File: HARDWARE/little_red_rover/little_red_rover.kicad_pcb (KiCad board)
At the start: 2 copper layers, 127.3 x 82.2 mm, 50 parts, among them J1 USB_C_Receptacle_USB2.0_14P, J2 Conn_01x04_Socket, J3 Conn_01x02_Socket, J4 Conn_01x02_Socket, J5 Conn_01x01_Socket, J6 Conn_01x01_Socket, U1 ESP32-C3-MINI-1, U2 BQ24230RGT, U3 MIC5504-3.3YM5, U4 TPS613222ADBV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

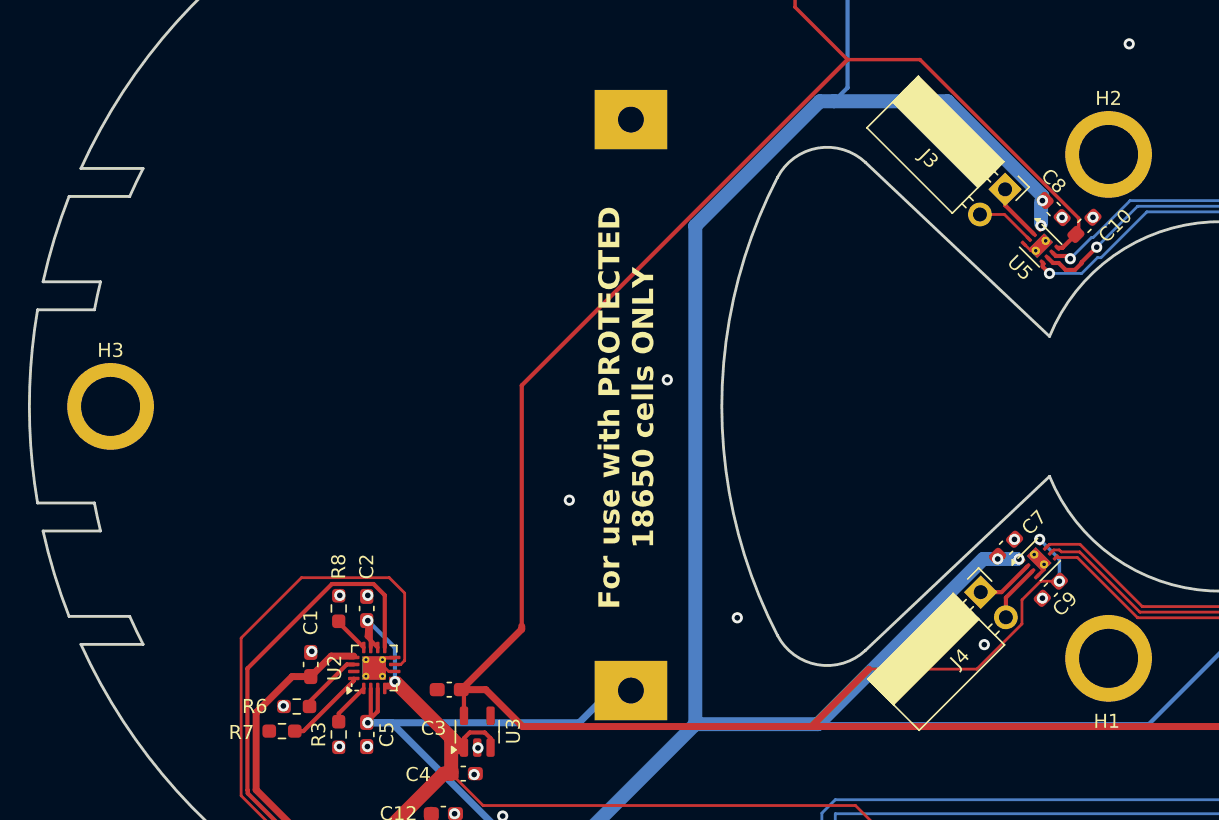
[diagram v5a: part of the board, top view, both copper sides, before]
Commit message: Fix threaded inserts not being included in BOM / placement
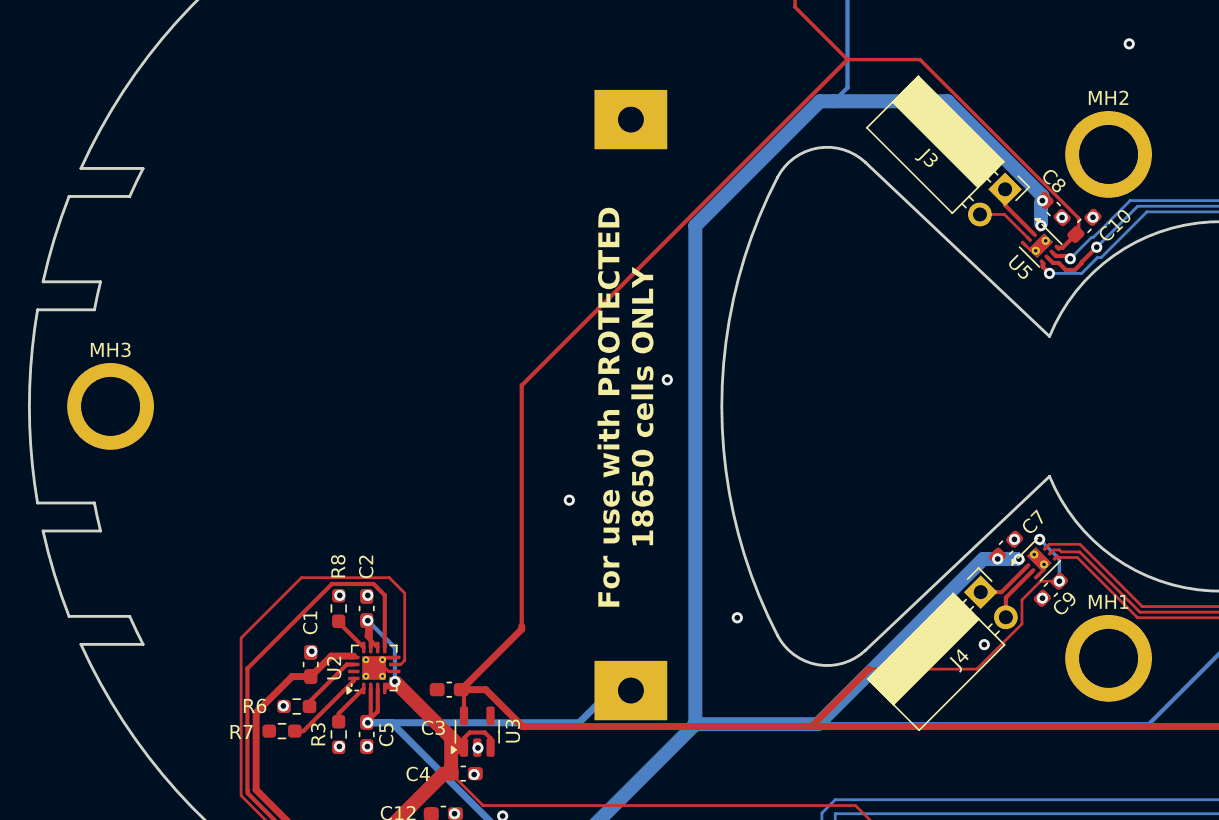
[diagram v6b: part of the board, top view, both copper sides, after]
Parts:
- removed H1, H2, H3: MountingHole, digikey_imports:m3_threaded_insert
- added MH1: M3_threaded, digikey_imports:m3_threaded_insert, F.Cu at (163.5, 117.9)
- added MH2: M3_threaded, digikey_imports:m3_threaded_insert, F.Cu at (163.5, 81.9)
- added MH3: M3_threaded, digikey_imports:m3_threaded_insert, F.Cu at (92.2, 99.9)
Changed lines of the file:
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@@
       (drillshape 0)
       (scaleselection 1)
-      (outputdirectory "gerbers/")
+      (outputdirectory "../pcb_fabrication_files/gerbers/")
     )
   )
@@
     (tags "capacitor handsolder")
     (property "JLC" "0603")
-    (property "LCSC" "C19666")
+    (property "LCSC" "")
     (property "Sheetfile" "little_red_rover.kicad_sch")
     (property "Sheetname" "")
@@
       (rotate (xyz 0 0 0))
     )
+  )
+  (footprint "digikey_imports:m3_threaded_insert" (layer "F.Cu")
+    (at 163.524805 117.9)
+    (property "JLC" "-")
+    (property "LCSC" "C5301780")
+    (property "Sheetfile" "little_red_rover.kicad_sch")
+    (property "Sheetname" "")
+    (property "ki_description" "Mounting Hole without connection")
+    (property "ki_keywords" "mounting hole")
+    (attr smd)
+    (fp_text reference "MH1" (at 0 -4 unlocked) (layer "F.SilkS")
+        (effects (font (size 1 1) (thickness 0.1)))
+    )
+    (fp_text value "M3_threaded" (at 0 4 unlocked) (layer "F.Fab")
+        (effects (font (size 1 1) (thickness 0.15)))
+    )
+    (fp_text user "${REFERENCE}" (at 0 6 unlocked) (layer "F.Fab")
+        (effects (font (size 1 1) (thickness 0.15)))
+    )
+    (pad "" np_thru_hole circle (at 0 0) (size 6.2 6.2) (drill 4.22) (layers "F&B.Cu" "*.Mask"))
   )
   (footprint "Capacitor_SMD:C_0603_1608Metric_Pad1.08x0.95mm_HandSolder" (layer "F.Cu")
@@
     (tags "capacitor handsolder")
     (property "JLC" "0603")
-    (property "LCSC" "C15849")
+    (property "LCSC" "")
     (property "Sheetfile" "little_red_rover.kicad_sch")
     (property "Sheetname" "")
@@
       (rotate (xyz 0 0 0))
     )
-  )
-  (footprint "digikey_imports:m3_threaded_insert" locked (layer "F.Cu")
-    (at 163.524805 81.9)
-    (property "JLC" "-")
-    (property "LCSC" "C5301780")
-    (property "Sheetfile" "little_red_rover.kicad_sch")
-    (property "Sheetname" "")
-    (property "ki_description" "Mounting Hole without connection")
-    (property "ki_keywords" "mounting hole")
-    (attr smd)
-    (fp_text reference "H2" (at 0 -4 unlocked) (layer "F.SilkS")
-        (effects (font (size 1 1) (thickness 0.1)))
-    )
-    (fp_text value "MountingHole" (at 0 4 unlocked) (layer "F.Fab")
-        (effects (font (size 1 1) (thickness 0.15)))
-    )
-    (fp_text user "${REFERENCE}" (at 0 6 unlocked) (layer "F.Fab")
-        (effects (font (size 1 1) (thickness 0.15)))
-    )
-    (pad "" np_thru_hole circle locked (at 0 0) (size 6.2 6.2) (drill 4.22) (layers "F&B.Cu" "*.Mask"))
   )
   (footprint "Resistor_SMD:R_0603_1608Metric_Pad0.98x0.95mm_HandSolder" (layer "F.Cu")
@@
     (tags "capacitor handsolder")
     (property "JLC" "0603")
-    (property "LCSC" "C19666")
+    (property "LCSC" "")
     (property "Sheetfile" "little_red_rover.kicad_sch")
     (property "Sheetname" "")
@@
     (tags "capacitor handsolder")
     (property "JLC" "0603")
-    (property "LCSC" "C15849")
+    (property "LCSC" "")
     (property "Sheetfile" "little_red_rover.kicad_sch")
     (property "Sheetname" "")
@@
     (tags "capacitor handsolder")
     (property "JLC" "0603")
-    (property "LCSC" "C19666")
+    (property "LCSC" "")
     (property "Sheetfile" "little_red_rover.kicad_sch")
     (property "Sheetname" "")
@@
     )
   )
+  (footprint "digikey_imports:m3_threaded_insert" (layer "F.Cu")
+    (at 163.524805 81.9)
+    (property "JLC" "-")
+    (property "LCSC" "C5301780")
+    (property "Sheetfile" "little_red_rover.kicad_sch")
+    (property "Sheetname" "")
+    (property "ki_description" "Mounting Hole without connection")
+    (property "ki_keywords" "mounting hole")
+    (attr smd)
+    (fp_text reference "MH2" (at 0 -4 unlocked) (layer "F.SilkS")
+        (effects (font (size 1 1) (thickness 0.1)))
+    )
+    (fp_text value "M3_threaded" (at 0 4 unlocked) (layer "F.Fab")
+        (effects (font (size 1 1) (thickness 0.15)))
+    )
+    (fp_text user "${REFERENCE}" (at 0 6 unlocked) (layer "F.Fab")
+        (effects (font (size 1 1) (thickness 0.15)))
+    )
+    (pad "" np_thru_hole circle (at 0 0) (size 6.2 6.2) (drill 4.22) (layers "F&B.Cu" "*.Mask"))
+  )
   (footprint "LED_SMD:LED_0603_1608Metric_Pad1.05x0.95mm_HandSolder" (layer "F.Cu")
     (at 154.9 137.8 90)
@@
     )
   )
-  (footprint "digikey_imports:m3_threaded_insert" locked (layer "F.Cu")
-    (at 163.524805 117.9)
-    (property "JLC" "-")
-    (property "LCSC" "C5301780")
-    (property "Sheetfile" "little_red_rover.kicad_sch")
-    (property "Sheetname" "")
-    (property "ki_description" "Mounting Hole without connection")
-    (property "ki_keywords" "mounting hole")
-    (attr smd)
-    (fp_text reference "H1" (at -0.124805 4.5 unlocked) (layer "F.SilkS")
-        (effects (font (size 1 1) (thickness 0.1)))
-    )
-    (fp_text value "MountingHole" (at 0 4 unlocked) (layer "F.Fab")
-        (effects (font (size 1 1) (thickness 0.15)))
-    )
-    (fp_text user "${REFERENCE}" (at 0 6 unlocked) (layer "F.Fab")
-        (effects (font (size 1 1) (thickness 0.15)))
-    )
-    (pad "" np_thru_hole circle locked (at 0 0) (size 6.2 6.2) (drill 4.22) (layers "F&B.Cu" "*.Mask"))
-  )
-  (footprint "digikey_imports:m3_threaded_insert" locked (layer "F.Cu")
-    (at 92.224805 99.9)
-    (property "JLC" "-")
-    (property "LCSC" "C5301780")
-    (property "Sheetfile" "little_red_rover.kicad_sch")
-    (property "Sheetname" "")
-    (property "ki_description" "Mounting Hole without connection")
-    (property "ki_keywords" "mounting hole")
-    (attr smd)
-    (fp_text reference "H3" (at 0 -4 unlocked) (layer "F.SilkS")
-        (effects (font (size 1 1) (thickness 0.1)))
-    )
-    (fp_text value "MountingHole" (at 0 4 unlocked) (layer "F.Fab")
-        (effects (font (size 1 1) (thickness 0.15)))
-    )
-    (fp_text user "${REFERENCE}" (at 0 6 unlocked) (layer "F.Fab")
-        (effects (font (size 1 1) (thickness 0.15)))
-    )
-    (pad "" np_thru_hole circle locked (at 0 0) (size 6.2 6.2) (drill 4.22) (layers "F&B.Cu" "*.Mask"))
-  )
   (footprint "Capacitor_SMD:C_0603_1608Metric_Pad1.08x0.95mm_HandSolder" (layer "F.Cu")
     (at 190 104.4 180)
@@
     (tags "capacitor handsolder")
     (property "JLC" "0603")
-    (property "LCSC" "C19666")
+    (property "LCSC" "")
     (property "Sheetfile" "little_red_rover.kicad_sch")
     (property "Sheetname" "")
@@
       (rotate (xyz 0 0 0))
     )
+  )
+  (footprint "digikey_imports:m3_threaded_insert" (layer "F.Cu")
+    (at 92.224805 99.9)
+    (property "JLC" "-")
+    (property "LCSC" "C5301780")
+    (property "Sheetfile" "little_red_rover.kicad_sch")
+    (property "Sheetname" "")
+    (property "ki_description" "Mounting Hole without connection")
+    (property "ki_keywords" "mounting hole")
+    (attr smd)
+    (fp_text reference "MH3" (at 0 -4 unlocked) (layer "F.SilkS")
+        (effects (font (size 1 1) (thickness 0.1)))
+    )
+    (fp_text value "M3_threaded" (at 0 4 unlocked) (layer "F.Fab")
+        (effects (font (size 1 1) (thickness 0.15)))
+    )
+    (fp_text user "${REFERENCE}" (at 0 6 unlocked) (layer "F.Fab")
+        (effects (font (size 1 1) (thickness 0.15)))
+    )
+    (pad "" np_thru_hole circle (at 0 0) (size 6.2 6.2) (drill 4.22) (layers "F&B.Cu" "*.Mask"))
   )
   (footprint "Resistor_SMD:R_0603_1608Metric_Pad0.98x0.95mm_HandSolder" (layer "F.Cu")
@@
     (descr "SOT, 5 Pin (https://www.jedec.org/sites/default/files/docs/Mo-178c.PDF variant AA), generated with kicad-footprint-generator ipc_gullwing_generator.py")
     (tags "SOT TO_SOT_SMD")
+    (property "JLC" "SOT-23-5")
+    (property "LCSC" "C2070802")
     (property "Sheetfile" "little_red_rover.kicad_sch")
     (property "Sheetname" "")
@@
     (tags "capacitor handsolder")
     (property "JLC" "0603")
-    (property "LCSC" "C15849")
-    (property "Sheetfile" "little_red_rover.kicad_sch")
-    (property "Sheetname" "")
+    (property "LCSC" "")
+    (property "Sheetfile" "little_red_rover.kicad_sch")
+    (property "Sheetname" "")

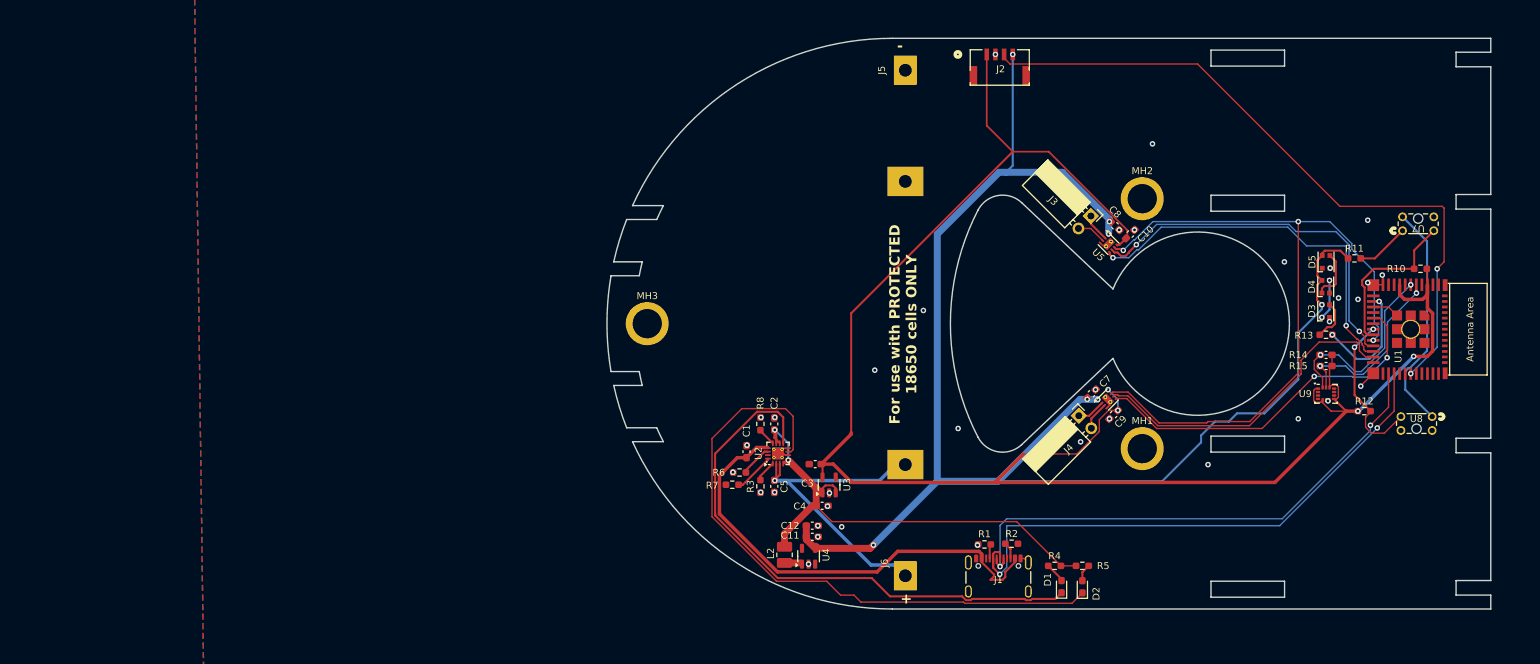
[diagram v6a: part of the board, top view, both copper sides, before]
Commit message: Update PCB layout: Position components for new schematic updates
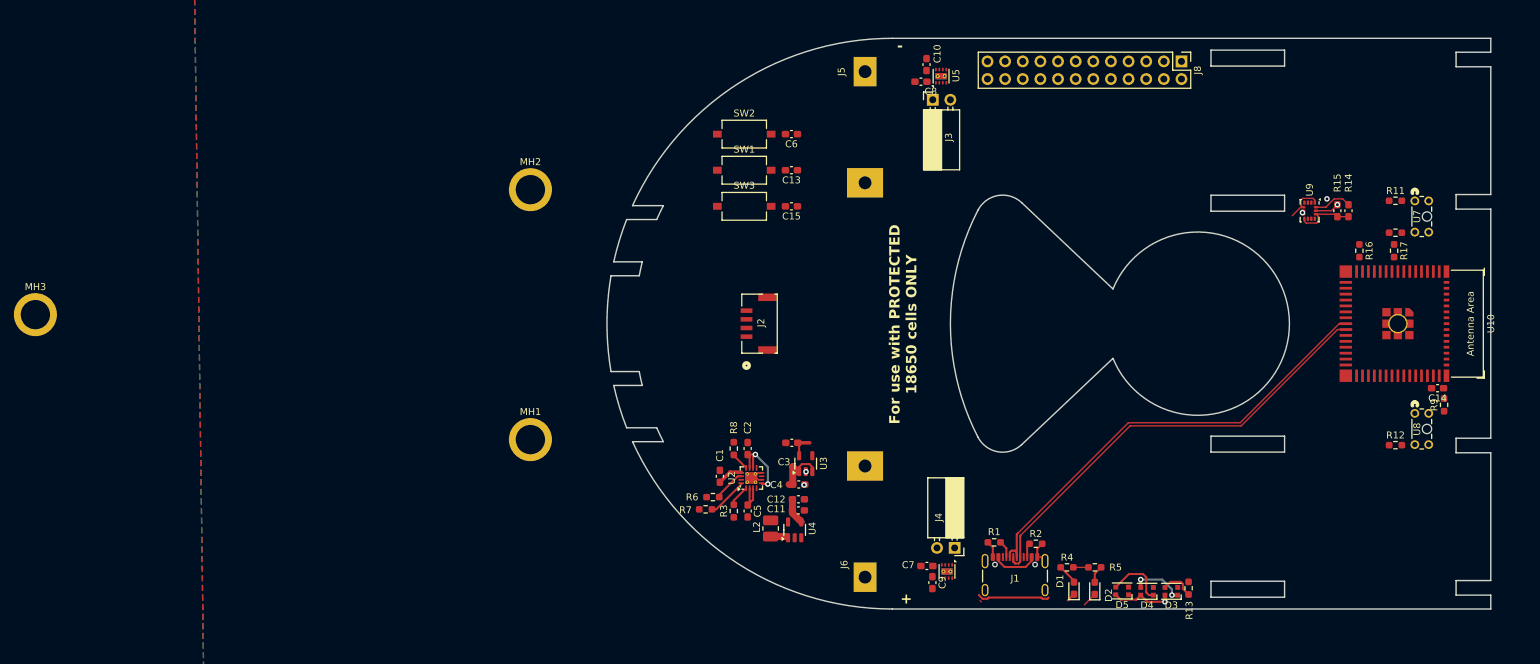
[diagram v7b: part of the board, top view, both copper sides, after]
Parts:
- removed G***: LOGO, digikey_imports:qr_code
- removed U1: ESP32-C3-MINI-1, Espressif:ESP32-C3-MINI-1_HandSoldering
- added C13: 0.1uF, Capacitor_SMD:C_0603_1608Metric_Pad1.08x0.95mm_HandSolder, F.Cu at (113.0, 77.8)
- added C14: 0.1uF, Capacitor_SMD:C_0603_1608Metric_Pad1.08x0.95mm_HandSolder, F.Cu at (206.1, 109.2)
- added C15: 0.1uF, Capacitor_SMD:C_0603_1608Metric_Pad1.08x0.95mm_HandSolder, F.Cu at (113.0, 83.0)
- added C6: 1uF, Capacitor_SMD:C_0603_1608Metric_Pad1.08x0.95mm_HandSolder, F.Cu at (113.0, 72.6)
- added J8: Conn_02x12_Odd_Even, Connector_PinHeader_2.54mm:PinHeader_2x12_P2.54mm_Vertical, F.Cu at (169.2, 62.1)
- added R16: 10k, Resistor_SMD:R_0603_1608Metric_Pad0.98x0.95mm_HandSolder, F.Cu at (194.8, 89.4)
- added R17: 10k, Resistor_SMD:R_0603_1608Metric_Pad0.98x0.95mm_HandSolder, F.Cu at (199.8, 89.4)
- added R9: 10k, Resistor_SMD:R_0603_1608Metric_Pad0.98x0.95mm_HandSolder, F.Cu at (207.0, 111.6)
- added SW1: SW_Push, Button_Switch_SMD:SW_Tactile_SPST_NO_Straight_CK_PTS636Sx25SMTRLFS, F.Cu at (106.2, 77.8)
- added SW2: SW_Push, Button_Switch_SMD:SW_Tactile_SPST_NO_Straight_CK_PTS636Sx25SMTRLFS, F.Cu at (106.2, 72.6)
- added SW3: SW_Push, Button_Switch_SMD:SW_Tactile_SPST_NO_Straight_CK_PTS636Sx25SMTRLFS, F.Cu at (106.2, 83.0)
- added U10: ESP32-S3-MINI-1, Espressif:ESP32-S2-MINI-1_HandSoldering, F.Cu at (200.3, 99.9)
- moved MH3 88.1 mm to (4.10, 98.6)
- moved MH1 88.1 mm to (75.4, 116.6)
- moved MH2 88.1 mm to (75.4, 80.6)
- moved D5 55.8 mm to (160.6, 138.4), turned to 180 degrees
- moved D4 50.9 mm to (164.2, 138.4), turned to 180 degrees
- moved J2 50.6 mm to (108.4, 99.9), turned to 90 degrees
- moved D3 46.1 mm to (167.7, 138.4), turned to 180 degrees
- moved R13 41.5 mm to (170.2, 138.0), turned to -90 degrees
- moved C10 38.2 mm to (132.4, 62.6), turned to 90 degrees
- moved C9 35.6 mm to (133.3, 137.2), turned to -90 degrees
- moved C8 34.8 mm to (131.7, 65.0), turned to 180 degrees
- moved C7 34.3 mm to (132.5, 134.8), turned to 180 degrees
- moved U5 34.2 mm to (134.6, 64.2), turned to 90 degrees
- moved U6 33.9 mm to (135.4, 135.6), turned to -90 degrees
- moved J3 28.3 mm to (133.3, 67.7), turned to 90 degrees
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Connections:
- J1 pad A6: /usb_data_- -> /usb_data_+
- J1 pad A7: /usb_data_+ -> /usb_data_-
- J1 pad B6: /usb_data_- -> /usb_data_+
- J1 pad B7: /usb_data_+ -> /usb_data_-
- U2 pad 4: /charger_out -> GND
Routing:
- net +3.3V: track 263.4 -> 17.7 mm, vias 4 -> 0
- net +5V: track 215.6 -> 13.1 mm, vias 7 -> 1
- net /motor_sleep: track 106.9 -> 0.00 mm, vias 3 -> 0
- net /lidar_tx: track 98.7 -> 0.00 mm, vias 2 -> 0
- net Net-(D2-K): track 90.0 -> 2.37 mm
- net Net-(D1-K): track 80.8 -> 11.8 mm
- net /usb_5v: track 67.0 -> 10.3 mm
- net /left_motor_pwm_b: track 55.0 -> 0.00 mm, vias 2 -> 0
- net /left_motor_pwm_a: track 54.2 -> 0.00 mm, vias 2 -> 0
- net /right_motor_pwm_b: track 52.2 -> 0.00 mm, vias 2 -> 1
- net /charger_out: track 72.1 -> 21.0 mm
- net /right_motor_pwm_a: track 46.9 -> 0.00 mm
- net Net-(J6-Pin_1): track 49.0 -> 4.78 mm, vias 1 -> 0
- net Net-(U7-CATHODE): track 33.3 -> 0.00 mm
- net /left_encoder: track 23.8 -> 0.00 mm
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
